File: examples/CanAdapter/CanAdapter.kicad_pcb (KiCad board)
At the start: 4 copper layers, 58.5 x 18 mm, 53 parts, among them J1 COM-15111 (Sparkfun), J2 SWD, J3 5023520500 (Molex), SW1 EVQ-P7C01P, SW2 EVQ-P7C01P, U1 AP2204K-3.3 (Diodes Incorpora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, U2 TPD2E009 (Texas Instruments), U3 LPC1549JBD48 (NXP), U4 ISO1050DUB (Texas Instruments), U5 QT096T_IF09, FH12-8S-0.5SH(55), U6 AP2204K-5.0 (Diodes Incorpora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, U7 PESD1CAN,215, U8 Duck, X1 7V-12.000MAHE-T (TXC)

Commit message: obdapter wip
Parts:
- removed 1: LeadFree, calisco:Indicator_LeadFree
- removed 2: IdDots4, calisco:Indicator_IdDots_4
- removed C1, C19: CL10A105KP8NNNC (Samsung Electro-Mechanics) - 1µF, 10V, Capacitor_SMD:C_0603_1608Metric
- removed C10, C12, C13, C17, C18, C3, C5, C7, C9: CL10B104KB8NNNC (Samsung Electro-Mechanics) - 0.1µF, 50V, Capacitor_SMD:C_0603_1608Metric
- removed C11, C14: CL21A106KPFNNNE (Samsung Electro-Mechanics) - 10µF, 10V, Capacitor_SMD:C_0805_2012Metric
- removed C15, C16: CC0603GRNPO9BN180 (Yageo) - 18pF, 50V, Capacitor_SMD:C_0603_1608Metric
- removed C2: CL21B225KPFNNNE (Samsung Electro-Mechanics) - 2.2µF, 10V, Capacitor_SMD:C_0805_2012Metric
- removed C20: CL10A105KA8NNNC (Samsung Electro-Mechanics) - 1µF, 25V, Capacitor_SMD:C_0603_1608Metric
- removed C21: CL31B225KOHNNNE (Samsung Electro-Mechanics) - 2.2µF, 16V, Capacitor_SMD:C_1206_3216Metric
- removed C4, C6, C8: CL10B103KB8NNNC (Samsung Electro-Mechanics) - 10000pF, 50V, Capacitor_SMD:C_0603_1608Metric
- removed D1, D2: EAST1616RGBB2 (Everlight Electronics Co Ltd), calisco:LED_RGB_0606
- removed D3: LED, LED_SMD:LED_0603_1608Metric
- removed J1: COM-15111 (Sparkfun), calisco:USB_C_Receptacle_BSC_A40-00119
- removed J2: SWD, Connector:Tag-Connect_TC2050-IDC-NL_2x05_P1.27mm_Vertical
- removed J3: 5023520500 (Molex), calisco:Molex_DuraClik_502352_1x05_P2.00mm_Horizontal
- removed R1, R2: 5.1k, 1%, 0.1W, Resistor_SMD:R_0603_1608Metric
- removed R10, R11, R12, R13, R7, R8, R9: 1k, 1%, 0.1W, Resistor_SMD:R_0603_1608Metric
- removed R3, R4, R5: 10k, 1%, 0.1W, Resistor_SMD:R_0603_1608Metric
- removed R6: 100, 1%, 0.1W, Resistor_SMD:R_0603_1608Metric
- removed SW1, SW2: EVQ-P7C01P, Button_Switch_SMD:SW_SPST_EVQP7C
- removed U1: AP2204K-3.3 (Diodes Incorporated), Package_TO_SOT_SMD:SOT-23-5
- removed U2: TPD2E009 (Texas Instruments), Package_TO_SOT_SMD:SOT-23
- removed U3: LPC1549JBD48 (NXP), Package_QFP:LQFP-48_7x7mm_P0.5mm
- removed U4: ISO1050DUB (Texas Instruments), Package_SO:SOP-8_6.62x9.15mm_P2.54mm
- removed U5: QT096T_IF09, FH12-8S-0.5SH(55), Connector_FFC-FPC:Hirose_FH12-8S-0.5SH_1x08-1MP_P0.50mm_Horizontal
- removed U6: AP2204K-5.0 (Diodes Incorporated), Package_TO_SOT_SMD:SOT-23-5
- removed U7: PESD1CAN,215, Package_TO_SOT_SMD:SOT-23
- removed U8: Duck, calisco:Symbol_Duckling
- removed X1: 7V-12.000MAHE-T (TXC), Oscillator:Oscillator_SMD_Abracon_ASE-4Pin_3.2x2.5mm
- added can.ic: SN65HVD230DR, Package_SO:SOIC-8_3.9x4.9mm_P1.27mm, F.Cu at (104.0, 102.0)
- added can.vdd_cap: 100nF, Capacitor_SMD:C_0603_1608Metric, F.Cu at (106.0, 108.0)
- added ledg.package: LED, LED_SMD:LED_0603_1608Metric, F.Cu at (115.0, 92.0)
- added ledg.res: 1k, 1%, 0.1 W, Resistor_SMD:R_0603_1608Metric, F.Cu at (113.0, 92.0)
- added ledr.package: LED, LED_SMD:LED_0603_1608Metric, F.Cu at (110.0, 92.0)
- added ledr.res: 1k, 1%, 0.1 W, Resistor_SMD:R_0603_1608Metric, F.Cu at (108.0, 92.0)
- added ledw.package: LED, LED_SMD:LED_0603_1608Metric, F.Cu at (120.0, 92.0)
- added ledw.res: 1k, 1%, 0.1 W, Resistor_SMD:R_0603_1608Metric, F.Cu at (118.0, 92.0)
- added mcu.en_pull.c: 1uF, Capacitor_SMD:C_0603_1608Metric, F.Cu at (102.0, 108.0)
- added mcu.en_pull.r: 10k, 1%, 0.1 W, Resistor_SMD:R_0603_1608Metric, F.Cu at (104.0, 108.0)
- added mcu.ic: ESP32-S3-WROOM-1-N16R8, RF_Module:ESP32-S3-WROOM-1, F.Cu at (87.0, 100.0)
- added mcu.prog: , Connector:Tag-Connect_TC2030-IDC-NL_2x03_P1.27mm_Vertical, F.Cu at (104.0, 94.0)
- added mcu.vcc_cap0: 22uF, Capacitor_SMD:C_1206_3216Metric, F.Cu at (90.0, 115.0)
- added mcu.vcc_cap1: 100nF, Capacitor_SMD:C_0603_1608Metric, F.Cu at (94.0, 118.0)
- added obd: , project:J1962, B.Cu at (100.0, 100.0)
- added prot_3v3: 5?A@1V 90? Single 3.53V~3.67V 200mW 3.6V SOD-323 Zener Diod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, Diode_SMD:D_SOD-323, F.Cu at (118.0, 105.0)
- added reg_3v3.boot_cap: 100nF, Capacitor_SMD:C_0603_1608Metric, F.Cu at (109.0, 96.0)
- added reg_3v3.en_res: 510k, 1%, 0.1 W, Resistor_SMD:R_0603_1608Metric, F.Cu at (111.0, 96.0)
- added reg_3v3.fb.bottom_res: 1.5k, 1%, 0.1 W, Resistor_SMD:R_0603_1608Metric, F.Cu at (115.0, 96.0)
- added reg_3v3.fb.top_res: 6.8k, 1%, 0.1 W, Resistor_SMD:R_0603_1608Metric, F.Cu at (113.0, 96.0)
- added reg_3v3.hf_in_cap: 100nF, Capacitor_SMD:C_0603_1608Metric, F.Cu at (113.0, 101.0)
- added reg_3v3.ic: TPS54202H, Package_TO_SOT_SMD:SOT-23-6, F.Cu at (110.0, 101.0)
- added reg_3v3.power_path.in_cap: 10uF, Capacitor_SMD:C_0805_2012Metric, F.Cu at (115.0, 101.0)
- added reg_3v3.power_path.inductor: 1.4A 22uH ±20% 126m? SMD Power Inductors ROHS, Inductor_SMD:L_Taiyo-Yuden_NR-50xx, F.Cu at (111.0, 107.0)
- added reg_3v3.power_path.out_cap: 10uF, Capacitor_SMD:C_0805_2012Metric, F.Cu at (115.0, 107.0)
- added vobd_sense.bottom_res: 10k, 1%, 0.1 W, Resistor_SMD:R_0603_1608Metric, F.Cu at (118.0, 97.0)
- added vobd_sense.top_res: 56k, 1%, 0.1 W, Resistor_SMD:R_0603_1608Metric, F.Cu at (118.0, 101.0)
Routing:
- net gnd: track 58.9 -> 12.8 mm, vias 8 -> 7
- net sw_can.out: track 35.1 -> 0.00 mm, vias 2 -> 0
- net v3v3: track 77.2 -> 49.6 mm, vias 14 -> 4
- net rgb_usb.package.blue_k: track 25.8 -> 0.00 mm, vias 2 -> 0
- net rgb_usb.package.red_k: track 21.0 -> 0.00 mm, vias 2 -> 0
- net can_esd.can.canh: track 20.7 -> 0.00 mm, vias 2 -> 0
- net mcu.can_0.rxd: track 19.2 -> 0.00 mm
- net mcu.swd.swclk: track 18.4 -> 0.00 mm, vias 3 -> 0
- net vobd: track 0.00 -> 18.4 mm, vias 0 -> 3
- net mcu.can_0.txd: track 18.0 -> 0.00 mm
- net vusb: track 17.7 -> 0.00 mm, vias 2 -> 0
- net rgb_can.blue: track 17.7 -> 0.00 mm, vias 1 -> 0
- net rgb_usb.package.green_k: track 17.6 -> 0.00 mm, vias 2 -> 0
- net mcu.digital_12: track 17.4 -> 0.00 mm, vias 1 -> 0
- net mcu.swd.swo: track 17.0 -> 0.00 mm, vias 2 -> 0
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- added copper zone on F.Cu, net reg_3v3.boot_cap.neg
- added copper zone on F.Cu, net v3v3
- removed copper zone on B.Cu, net can_gnd
- removed copper zone on F.Cu, net can_gnd
- removed copper zone on In1.Cu, net can_gnd
- removed copper zone on In2.Cu, net can_reg.pwr_out
- removed copper zone on B.Cu, net gnd
- removed copper zone on F.Cu, net gnd
- removed copper zone on In1.Cu, net gnd
- removed copper zone on In2.Cu, net v3v3
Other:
- board size 58.5 x 18 mm -> 86 x 62 mm
- copper layers 4 -> 2
- rule pad_to_mask_clearance: 0.051 -> 0
- board text added: "OBDapter Apr '25 rv1"
- board text removed: "CAN Adapter v2"

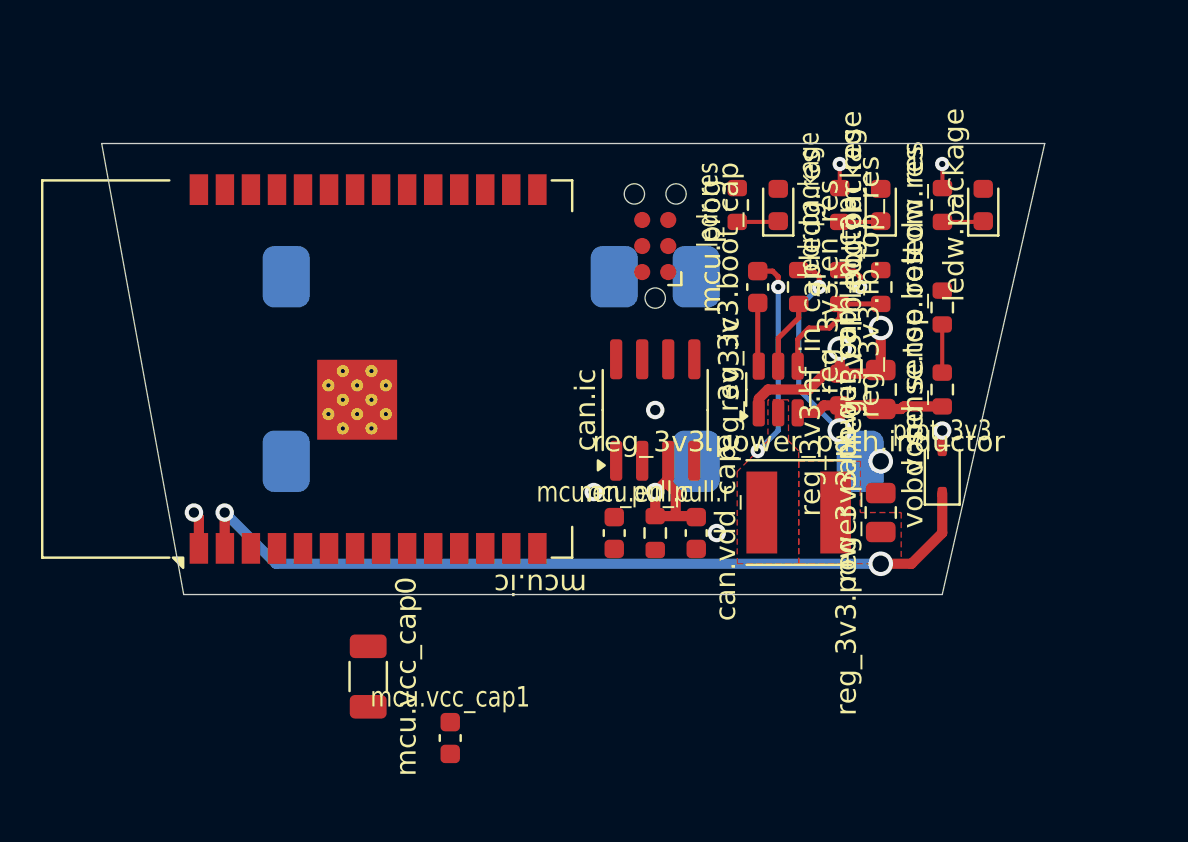
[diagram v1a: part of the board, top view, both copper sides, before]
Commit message: Update CanAdapter.kicad_pcb
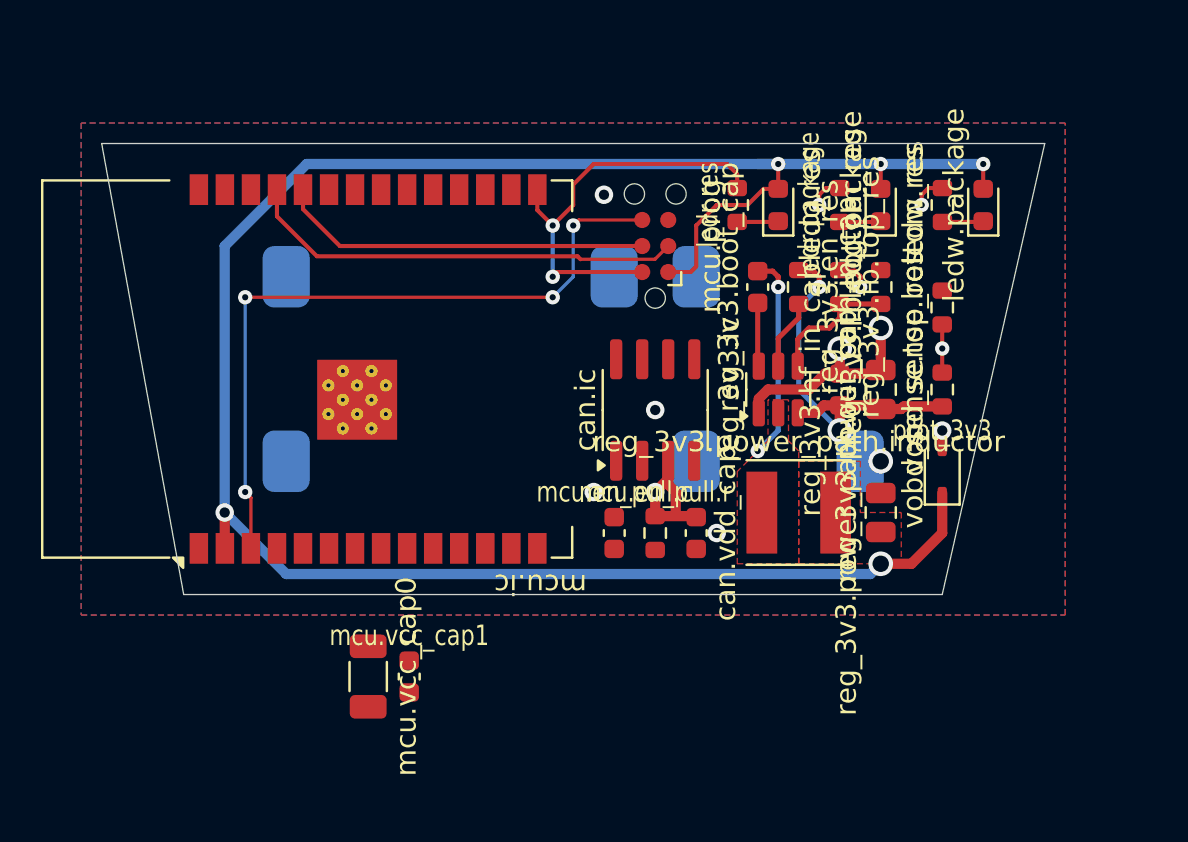
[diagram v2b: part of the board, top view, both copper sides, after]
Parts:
- moved mcu.vcc_cap1 3.61 mm to (92.0, 115.0)
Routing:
- net v3v3: track 49.6 -> 114.6 mm, vias 4 -> 7
- net mcu.program_en_node: track 0.00 -> 34.8 mm, vias 0 -> 4
- net mcu.program_uart_node.a_tx: track 0.00 -> 21.5 mm
- net mcu.program_boot_node: track 0.00 -> 20.7 mm, vias 0 -> 2
- net mcu.program_uart_node.b_tx: track 0.00 -> 18.2 mm
- net gnd: track 12.8 -> 10.9 mm
- net vobd_sense.output: vias 0 -> 1
- added copper zone on B.Cu, net gnd
- added copper zone on F.Cu, net gnd

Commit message: checkpoint
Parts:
- C3: renamed from reg_3v3.power_path.in_cap; footprint Capacitor_SMD:C_0805_2012Metric -> Capacitor_SMD:C_1210_3225Metric
- C5: renamed from mcu.vcc_cap0; value 22uF -> 10uF; footprint Capacitor_SMD:C_1206_3216Metric -> Capacitor_SMD:C_0805_2012Metric
- L1: renamed from reg_3v3.power_path.inductor; value 1.4A 22uH ±20% 126m? SMD Power Inductors ROHS -> 620mA 22uH ±10% 270m? 1210 Inductors (SMD) ROHS; footprint Inductor_SMD:L_Taiyo-Yuden_NR-50xx -> Inductor_SMD:L_1210_3225Metric
- R8: renamed from vobd_sense.top_res; value 56k, 1%, 0.1 W -> 100k, 1%, 0.1 W
- U3: renamed from mcu.ic; value ESP32-S3-WROOM-1-N16R8 -> ESP32-C3-WROOM-02; footprint RF_Module:ESP32-S3-WROOM-1 -> RF_Module:ESP-WROOM-02
- moved D1 22.0 mm to (96.0, 104.0), turned to -90 degrees
- moved R8 17.7 mm to (101.0, 96.0)
- moved R9 17.7 mm to (101.0, 92.0)
- moved C5 10.6 mm to (98.0, 108.0), turned to 90 degrees
- moved C6 8.06 mm to (96.0, 108.0)
- moved R4 7.21 mm to (98.0, 104.0)
- moved J1 7.00 mm to (97.0, 94.0)
- moved C8 6.00 mm to (100.0, 108.0), turned to 90 degrees
- moved C7 4.47 mm to (100.0, 104.0)
- moved U4 4.00 mm to (104.0, 106.0)
- moved C3 2.24 mm to (116.0, 103.0)
- moved C1 2.00 mm to (113.0, 103.0)
- moved C2 2.00 mm to (109.0, 98.0)
- moved R1 2.00 mm to (113.0, 98.0)
- moved R2 2.00 mm to (115.0, 98.0)
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- renumbered reg_3v3.hf_in_cap to C1, reg_3v3.boot_cap to C2, reg_3v3.power_path.out_cap to C4, mcu.vcc_cap1 to C6, mcu.en_pull.c to C7, can.vdd_cap to C8, prot_3v3 to D1, ledr.package to D2, ledg.package to D3, ledw.package to D4, mcu.prog to J1, reg_3v3.fb.top_res to R1, reg_3v3.fb.bottom_res to R2, reg_3v3.en_res to R3, mcu.en_pull.r to R4, ledr.res to R5, ledg.res to R6, ledw.res to R7, vobd_sense.bottom_res to R9, obd to U1, reg_3v3.ic to U2, can.ic to U4
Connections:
- D3 pad 2: v3v3 -> ledg.signal
- D4 pad 2: v3v3 -> ledw.signal
- R6 pad 2: ledg.signal -> gnd
- R7 pad 2: ledw.signal -> gnd
- U3 pad 1: gnd -> v3v3
- U3 pad 11: (no net) -> mcu.program_uart_node.b_tx
- U3 pad 12: (no net) -> mcu.program_uart_node.a_tx
- U3 pad 2: v3v3 -> mcu.program_en_node
- U3 pad 3: mcu.program_en_node -> can.controller.txd
- U3 pad 4: can.controller.txd -> can.controller.rxd
- U3 pad 5: can.controller.rxd -> (no net)
- U3 pad 7: (no net) -> v3v3
- U3 pad 8: (no net) -> mcu.program_boot_node
- U3 pad 9: (no net) -> gnd
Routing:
- net v3v3: track 114.6 -> 132.1 mm, vias 7 -> 9
- net mcu.program_en_node: track 34.8 -> 51.8 mm, vias 4 -> 3
- net mcu.program_boot_node: track 20.7 -> 36.3 mm
- net mcu.program_uart_node.b_tx: track 18.2 -> 6.19 mm
- net mcu.program_uart_node.a_tx: track 21.5 -> 9.50 mm
- net can.can.canh: track 0.00 -> 9.12 mm, vias 0 -> 1
- net can.can.canl: track 0.00 -> 3.09 mm, vias 0 -> 1
- net vobd_sense.output: track 2.35 -> 0.00 mm, vias 1 -> 0
- net gnd: track 10.9 -> 12.9 mm, vias 7 -> 5
- net vobd: track 18.4 -> 16.6 mm, vias 3 -> 2
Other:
- board size 86 x 62 mm -> 46 x 22 mm

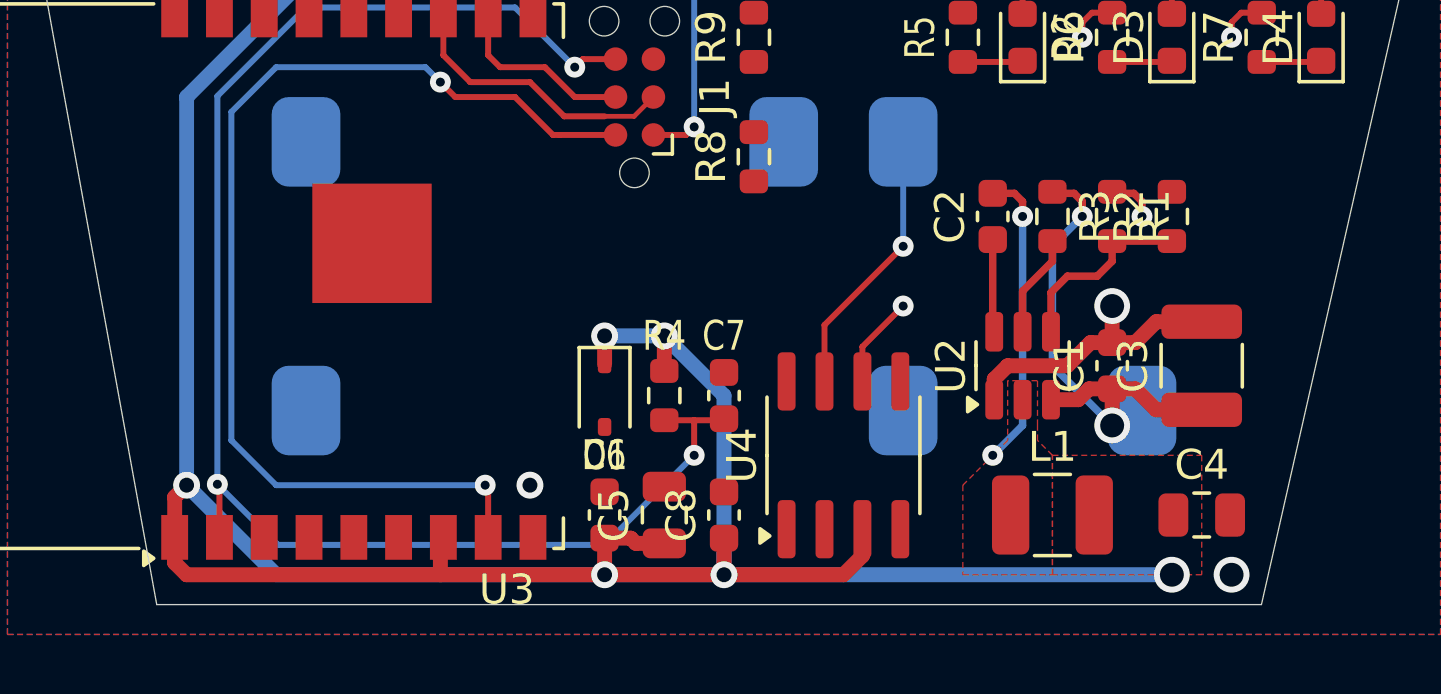
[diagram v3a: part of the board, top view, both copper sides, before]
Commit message: wip smaller inductor
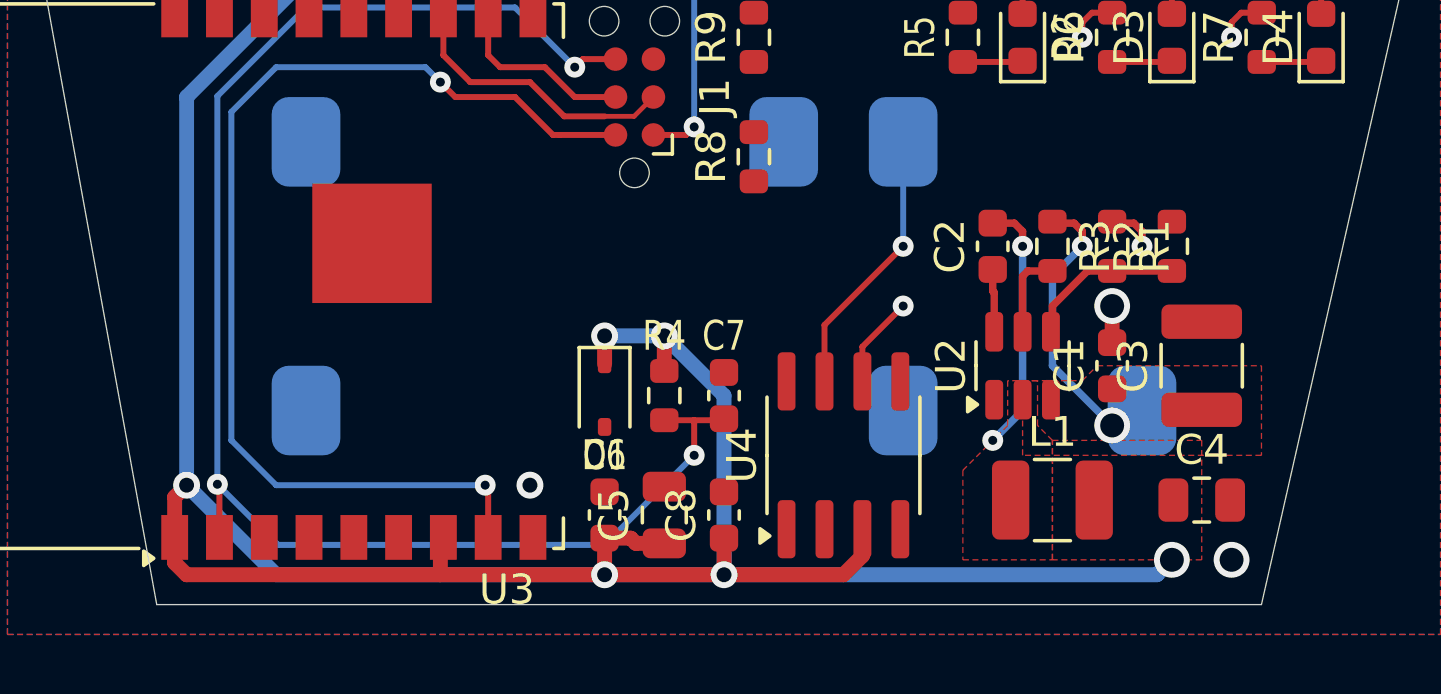
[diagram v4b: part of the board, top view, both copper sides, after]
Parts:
- moved C2 1.00 mm to (109.0, 99.0)
- moved R1 1.00 mm to (113.0, 99.0)
- moved R2 1.00 mm to (115.0, 99.0)
- moved R3 1.00 mm to (111.0, 99.0)
- moved C4 0.50 mm to (116.0, 107.5)
- moved L1 0.50 mm to (111.0, 107.5)
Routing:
- net gnd: track 12.9 -> 4.50 mm
- net vobd: track 16.6 -> 8.86 mm
- net reg_3v3.boot_cap.neg: track 10.0 -> 8.53 mm
- net reg_3v3.fb.output: track 6.47 -> 4.99 mm
- net reg_3v3.boot_cap.pos: track 3.04 -> 2.11 mm
- net reg_3v3.en_res.b: track 3.45 -> 2.93 mm
- added copper zone on F.Cu, net vobd

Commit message: done!
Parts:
- removed D4: LED, LED_SMD:LED_0603_1608Metric
- removed R7: 1k, 1%, 0.1 W, Resistor_SMD:R_0603_1608Metric
- added OD4: LED, LED_SMD:LED_0603_1608Metric, F.Cu at (118.0, 92.0)
- added OR7: 1k, 1%, 0.1 W, Resistor_SMD:R_0603_1608Metric, F.Cu at (120.0, 92.0)
- moved OR9 7.07 mm to (102.0, 99.0)
- moved OR8 4.24 mm to (104.0, 99.0), turned to -90 degrees
- moved OD2 2.00 mm to (108.0, 92.0), turned to -90 degrees
- moved OD3 2.00 mm to (113.0, 92.0), turned to -90 degrees
- moved OR5 2.00 mm to (110.0, 92.0), turned to -90 degrees
- moved OR6 2.00 mm to (115.0, 92.0), turned to -90 degrees
- renumbered C1 to OC1, C2 to OC2, C3 to OC3, C4 to OC4, C5 to OC5, C6 to OC6, C7 to OC7, C8 to OC8, D1 to OD1, D2 to OD2, D3 to OD3, J1 to OJ1, L1 to OL1, R1 to OR1, R2 to OR2, R3 to OR3, R4 to OR4, R5 to OR5, R6 to OR6, R8 to OR8, R9 to OR9, U1 to OU1, U2 to OU2, U3 to OU3, U4 to OU4
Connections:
- net can.can.canh renamed Ocan.can.canh
- net can.can.canl renamed Ocan.can.canl
- net gnd renamed Ognd
- net ledg.res.a renamed Oledg.res.a
- net ledr.res.a renamed Oledr.res.a
- net mcu.program_boot_node renamed Omcu.program_boot_node
- net mcu.program_en_node renamed Omcu.program_en_node
- net mcu.program_uart_node.a_tx renamed Omcu.program_uart_node.a_tx
- net mcu.program_uart_node.b_tx renamed Omcu.program_uart_node.b_tx
- net reg_3v3.boot_cap.neg renamed Oreg_3v3.boot_cap.neg
- net reg_3v3.boot_cap.pos renamed Oreg_3v3.boot_cap.pos
- net reg_3v3.en_res.b renamed Oreg_3v3.en_res.b
- net reg_3v3.fb.output renamed Oreg_3v3.fb.output
- net v3v3 renamed Ov3v3
- net vobd renamed Ovobd
- OD3 pad 2: ledg.signal -> Oledg.signal
- OR8 pad 2: vobd_sense.output -> Ovobd_sense.output
- OR9 pad 1: vobd_sense.output -> Ovobd_sense.output
- OU3 pad 13: (no net) -> Oledg.signal
- OU3 pad 14: (no net) -> Oledw.signal
- OU3 pad 15: ledw.signal -> (no net)
- OU3 pad 17: ledg.signal -> (no net)
- OU3 pad 18: vobd_sense.output -> (no net)
- OU3 pad 3: can.controller.txd -> (no net)
- OU3 pad 4: can.controller.rxd -> Ovobd_sense.output
- OU3 pad 5: (no net) -> Ocan.controller.rxd
- OU3 pad 6: (no net) -> Ocan.controller.txd
- OU4 pad 1: can.controller.txd -> Ocan.controller.txd
- OU4 pad 4: can.controller.rxd -> Ocan.controller.rxd
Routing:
- net Oledw.signal: track 0.00 -> 37.3 mm
- net Oledg.signal: track 0.00 -> 30.6 mm
- net Ocan.controller.rxd: track 0.00 -> 26.7 mm, vias 0 -> 2
- net Ovobd_sense.output: track 0.00 -> 24.1 mm
- net Ocan.controller.txd: track 0.00 -> 22.7 mm, vias 0 -> 2
- net Omcu.program_boot_node: track 36.3 -> 55.7 mm
- net Ov3v3: track 132.3 -> 145.0 mm, vias 9 -> 10
- net Ovobd: track 8.86 -> 17.6 mm
- net Ocan.can.canl: track 3.09 -> 6.59 mm
- net Ognd: track 4.50 -> 7.23 mm, vias 5 -> 8
- net Oledw.res.a: track 0.00 -> 2.02 mm
- net ledw.res.a: track 2.01 -> 0.00 mm
- net ledw.signal: track 1.21 -> 0.00 mm, vias 1 -> 0
- net ledg.signal: track 1.21 -> 0.00 mm, vias 1 -> 0
- net Omcu.program_en_node: track 51.8 -> 52.3 mm
